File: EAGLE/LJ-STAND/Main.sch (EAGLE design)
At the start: 121 parts

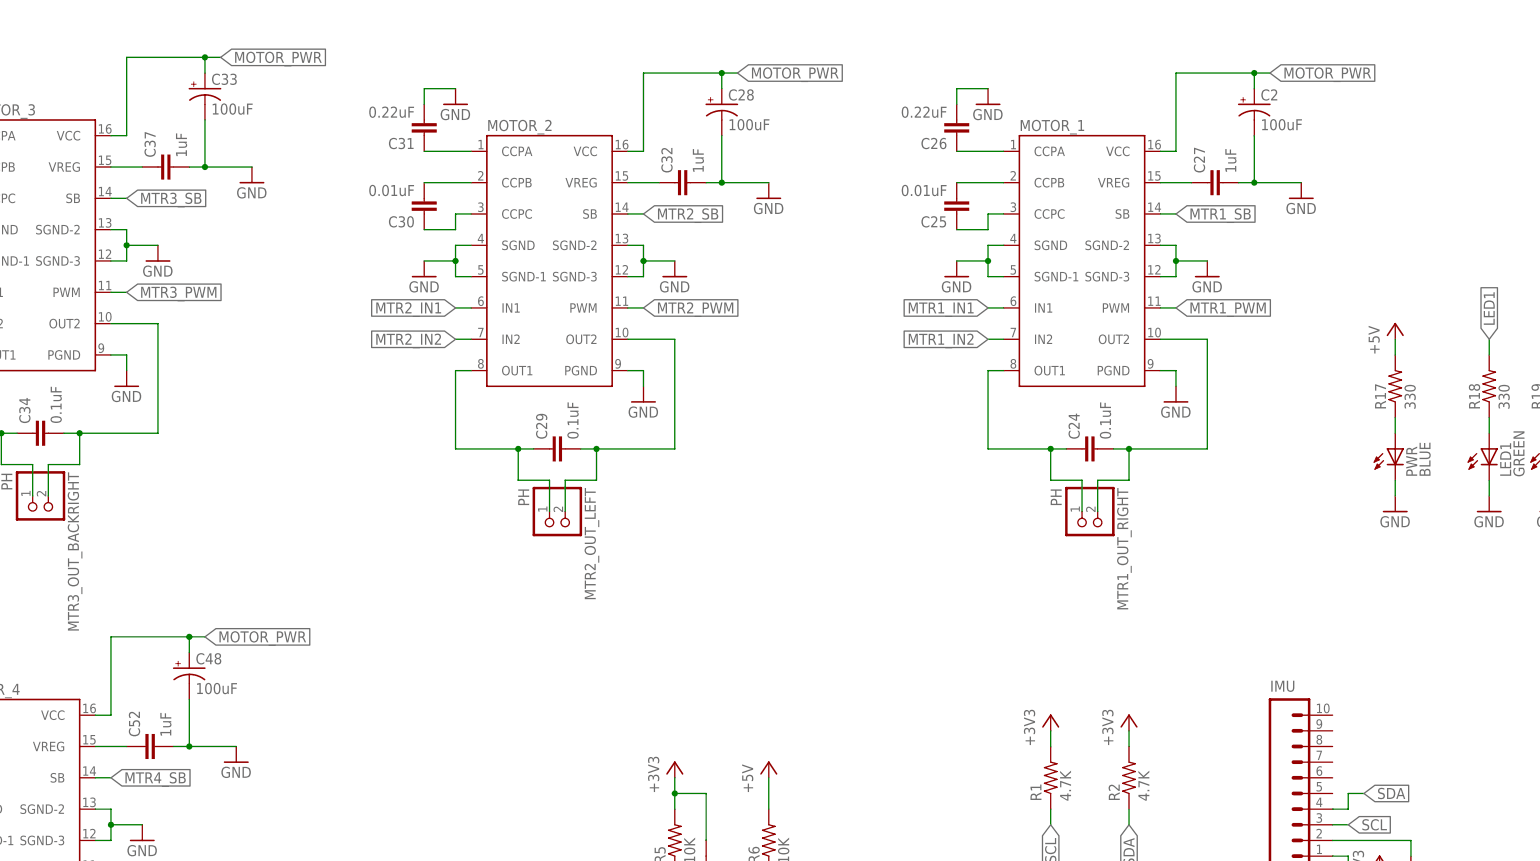
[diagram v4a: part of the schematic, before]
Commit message: Filtering cap on motor controllers
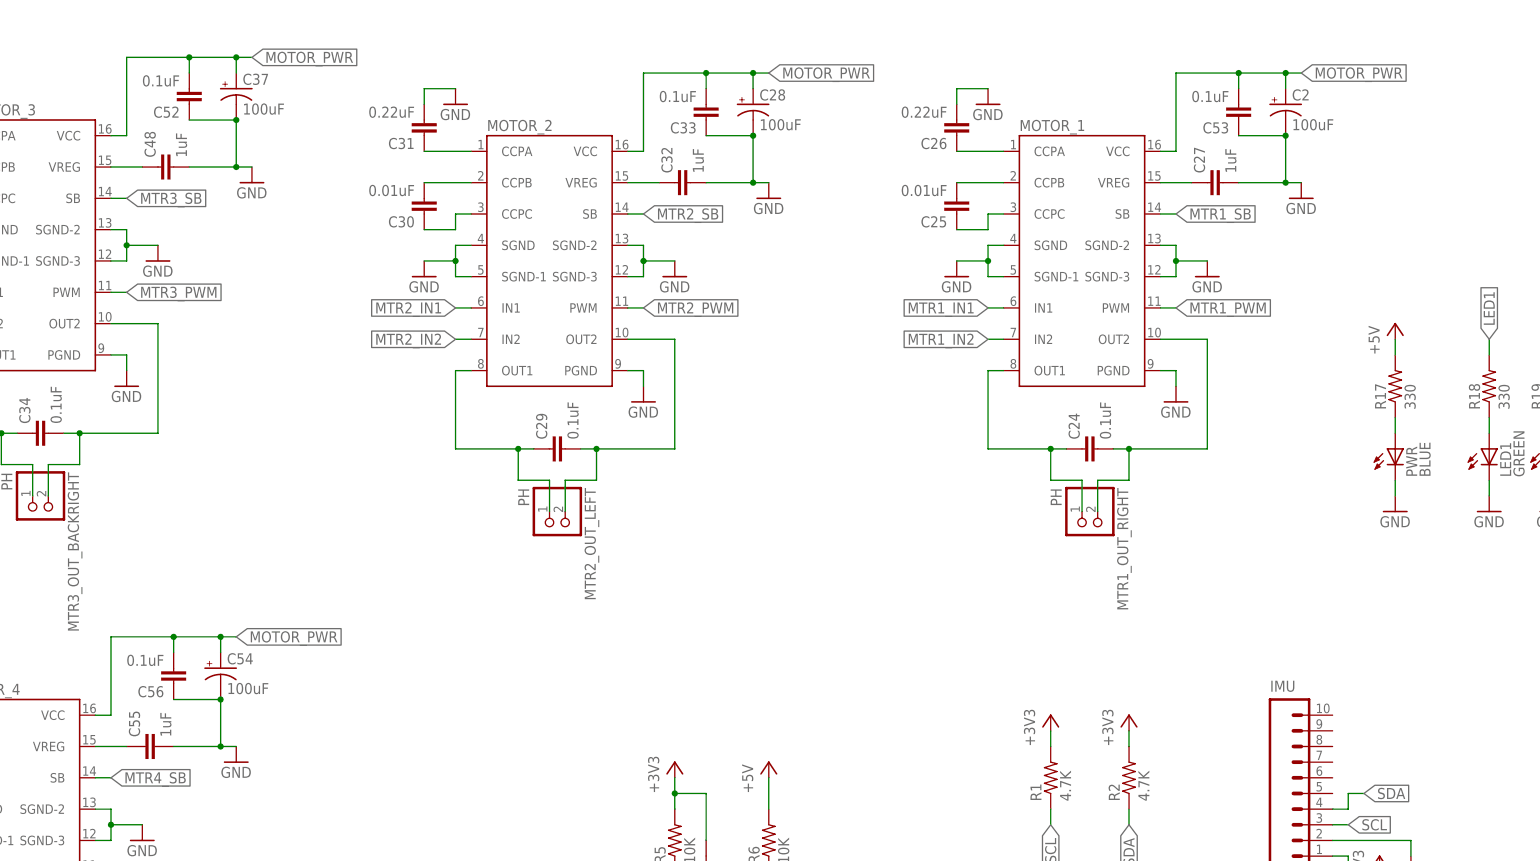
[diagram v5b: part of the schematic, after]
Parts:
- added C53, C56: 0.1uF, SparkFun-Capacitors:CAP0603-CAP
- added C54: 100uF, SparkFun-Capacitors:CAP_POLPTH1
- added C55: 1uF, SparkFun-Capacitors:CAP0603-CAP
- C33: value 100uF -> 0.1uF; device SparkFun-Capacitors:CAP_POLPTH1 -> SparkFun-Capacitors:CAP0603-CAP
- C37: value 1uF -> 100uF; device SparkFun-Capacitors:CAP0603-CAP -> SparkFun-Capacitors:CAP_POLPTH1
- C48: value 100uF -> 1uF; device SparkFun-Capacitors:CAP_POLPTH1 -> SparkFun-Capacitors:CAP0603-CAP
- C52: value 1uF -> 0.1uF
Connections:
- net GND: now also C33.1, C37.-, C48.2, C52.1, C53.1, C54.-, C55.2, C56.1; no longer C33.-, C37.2, C48.-, C52.2
- net MOTOR_PWR: now also C33.2, C37.+, C52.2, C53.2, C54.+, C56.2; no longer C33.+, C48.+, MOTOR_2.VCC, MOTOR_3.VCC, MOTOR_4.VCC
- net N$20: now also C48.1; no longer C37.1, MOTOR_3.VREG
- net N$32: now also C55.1; no longer C52.1, MOTOR_4.VREG
- net N$8: no longer MOTOR_2.VREG
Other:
- moved on the sheet: C2, C28, C52

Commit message: Diode
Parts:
- added D1: (no value), diode:SCHOTTKY-DIODEP6T15
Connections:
- new net N$35: C1.+, D1.A, PWR_IN.2
- net PWR: now also D1.C; no longer C1.+, PWR_IN.2
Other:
- moved on the sheet: PWR_IN
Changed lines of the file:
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@@
 <part name="C55" library="SparkFun-Capacitors" deviceset="CAP" device="0603-CAP" value="1uF"/>
 <part name="C56" library="SparkFun-Capacitors" deviceset="CAP" device="0603-CAP" value="0.1uF"/>
+<part name="D1" library="diode" deviceset="SCHOTTKY-DIODE" device="P6T15"/>
 </parts>
 <sheets>
@@
 <instance part="GND9" gate="1" x="76.2" y="96.52"/>
 <instance part="+3V1" gate="G$1" x="93.98" y="119.38"/>
-<instance part="PWR_IN" gate="G$1" x="-48.26" y="121.92" rot="R180"/>
+<instance part="PWR_IN" gate="G$1" x="-50.8" y="121.92" rot="R180"/>
 <instance part="C13" gate="G$1" x="60.96" y="106.68"/>
 <instance part="C14" gate="G$1" x="91.44" y="106.68"/>
@@
 <instance part="C55" gate="G$1" x="12.7" y="254" rot="R90"/>
 <instance part="C56" gate="G$1" x="15.24" y="266.7" rot="R180"/>
+<instance part="D1" gate="G$1" x="-30.48" y="124.46"/>
 </instances>
 <busses>
@@
 <net name="PWR" class="0">
 <segment>
-<pinref part="C1" gate="G$1" pin="+"/>
-<wire x1="-38.1" y1="124.46" x2="-25.4" y2="124.46" width="0.1524" layer="91"/>
-<wire x1="-25.4" y1="124.46" x2="-25.4" y2="132.08" width="0.1524" layer="91"/>
-<junction x="-38.1" y="124.46"/>
 <wire x1="-22.86" y1="132.08" x2="-25.4" y2="132.08" width="0.1524" layer="91"/>
+<wire x1="-25.4" y1="132.08" x2="-25.4" y2="124.46" width="0.1524" layer="91"/>
 <wire x1="-25.4" y1="124.46" x2="-25.4" y2="114.3" width="0.1524" layer="91"/>
-<junction x="-25.4" y="124.46"/>
 <wire x1="-25.4" y1="114.3" x2="-22.86" y2="114.3" width="0.1524" layer="91"/>
-<pinref part="PWR_IN" gate="G$1" pin="2"/>
-<wire x1="-48.26" y1="124.46" x2="-38.1" y2="124.46" width="0.1524" layer="91"/>
 <pinref part="MOTOR_FUSE" gate="G$1" pin="P1"/>
 <pinref part="LOGIC_FUSE" gate="G$1" pin="P1"/>
+<pinref part="D1" gate="G$1" pin="C"/>
+<wire x1="-27.94" y1="124.46" x2="-25.4" y2="124.46" width="0.1524" layer="91"/>
+<junction x="-25.4" y="124.46"/>
 </segment>
 </net>
@@
 <pinref part="PWR_IN" gate="G$1" pin="1"/>
 <wire x1="-43.18" y1="116.84" x2="-43.18" y2="121.92" width="0.1524" layer="91"/>
-<wire x1="-43.18" y1="121.92" x2="-48.26" y2="121.92" width="0.1524" layer="91"/>
+<wire x1="-43.18" y1="121.92" x2="-50.8" y2="121.92" width="0.1524" layer="91"/>
 </segment>
 <segment>
@@
 </segment>
 </net>
+<net name="N$35" class="0">
+<segment>
+<pinref part="C1" gate="G$1" pin="+"/>
+<pinref part="PWR_IN" gate="G$1" pin="2"/>
+<wire x1="-50.8" y1="124.46" x2="-38.1" y2="124.46" width="0.1524" layer="91"/>
+<pinref part="D1" gate="G$1" pin="A"/>
+<wire x1="-38.1" y1="124.46" x2="-33.02" y2="124.46" width="0.1524" layer="91"/>
+<junction x="-38.1" y="124.46"/>
+</segment>
+</net>

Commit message: Schematic things, removed main board file :/
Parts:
- PIXY_I2C, PIXY_SPI: device SparkFun-Connectors:M05X2SHD -> pinhead+:PINHD-2X5SMT
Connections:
- removed net XBEE_RX: MASTER.48/TX6
- removed net XBEE_TX: MASTER.47/RX6
- net MOTOR_PWR: now also MOTOR_2.VCC, MOTOR_3.VCC, MOTOR_4.VCC
- net N$20: now also C55.1, MOTOR_4.VREG; no longer C48.1
- net N$32: now also C32.1, MOTOR_2.VREG; no longer C55.1
- net N$8: now also C48.1, MOTOR_3.VREG; no longer C32.1
